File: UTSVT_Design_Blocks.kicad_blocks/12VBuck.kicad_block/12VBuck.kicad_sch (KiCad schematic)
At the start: 9 parts, among them U3 LMR51635XDDCR

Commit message: buck
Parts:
- C11: LCSC # C1607 -> (none); LCSC P/N (none) -> C1607; P/N (none) -> 581-0603YC225MAT2A
- C12: footprint Capacitor_SMD:C_0603_1608Metric_Pad1.08x0.95mm_HandSolder -> Resistor_SMD:R_0201_0603Metric_Pad0.64x0.40mm_HandSolder; LCSC # C440198 -> (none); LCSC P/N (none) -> C14663
- C13: footprint (none) -> Capacitor_SMD:C_0603_1608Metric_Pad1.08x0.95mm_HandSolder
- C14: footprint Capacitor_SMD:C_1210_3225Metric_Pad1.33x2.70mm_HandSolder -> Capacitor_SMD:C_0805_2012Metric_Pad1.18x1.45mm_HandSolder; LCSC P/N (none) -> C440198; P/N 81-GGM32ED70J476KE2L -> GRM21BR61H106KE43K
- C15: footprint Capacitor_SMD:C_1210_3225Metric_Pad1.33x2.70mm_HandSolder -> Capacitor_SMD:C_0805_2012Metric_Pad1.18x1.45mm_HandSolder; LCSC P/N (none) -> C5674; P/N 81-GGM32ED70J476KE2L -> 603-CC805MFX5R5BB226
- L3: footprint Inductor_SMD:L_Sunlord_SWPA4020S -> Inductor_SMD:L_Cenker_CKCS4030; LCSC # C88247 -> (none); LCSC P/N (none) -> C354591; P/N (none) -> 504-HPAL1V1265-150-R
- R1: value 143 -> 143k; footprint Resistor_SMD:R_0805_2012Metric_Pad1.20x1.40mm_HandSolder -> Resistor_SMD:R_0201_0603Metric_Pad0.64x0.40mm_HandSolder; LCSC P/N (none) -> C22877; P/N 667-ERJ-UP6F1430V -> 603-RT0603DRE07143KL; now fitted
- R4: footprint Capacitor_SMD:C_0402_1005Metric_Pad0.74x0.62mm_HandSolder -> Resistor_SMD:R_0201_0603Metric_Pad0.64x0.40mm_HandSolder; LCSC # C11660 -> (none); LCSC P/N (none) -> C22772; P/N (none) -> 603-RT0603DRE0710K2L; now fitted
- U3: LCSC P/N (none) -> C42432812; P/N (none) -> 595-LMR51635XDDCR
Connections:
- net V_in renamed V_in_24V
- net V_out renamed V_out_12V

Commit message: made changes
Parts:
- removed C13: C_Small, Capacitor_SMD:C_0603_1608Metric_Pad1.08x0.95mm_HandSolder, symbol Device:C_Small
- removed C14: 10u, Capacitor_SMD:C_0805_2012Metric_Pad1.18x1.45mm_HandSolder, symbol Device:C_Small
- removed C15: 22u, Capacitor_SMD:C_0805_2012Metric_Pad1.18x1.45mm_HandSolder, symbol Device:C_Small
- added C10, C9: 47u, Capacitor_SMD:C_1210_3225Metric_Pad1.33x2.70mm_HandSolder, symbol Device:C_Small
- C11: footprint Capacitor_SMD:C_0603_1608Metric_Pad1.08x0.95mm_HandSolder -> Capacitor_SMD:C_0805_2012Metric_Pad1.18x1.45mm_HandSolder; LCSC P/N C1607 -> C1771; P/N 581-0603YC225MAT2A -> 963-T21GCB7225MTPA1J
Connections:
- net GND: now also C10.2, C9.2
- net V_out_12V: now also C10.1, C9.1
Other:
- moved on the sheet: R1, R4

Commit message: review addressed
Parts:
- C10, C9: P/N 963-MLAST32MAB5476MP -> GRM32ER61C476KE15L
- C11: P/N 963-T21GCB7225MTPA1J -> CL21F225ZAFNNNE
- L3: footprint Inductor_SMD:L_Cenker_CKCS4030 -> Inductor_SMD:L_TDK_VLP8040; LCSC P/N C354591 -> C2849555; P/N 504-HPAL1V1265-150-R -> PNLS8040-150M 15UH
- R1: P/N 603-RT0603DRE07143KL -> 0603WAF1433T5E
- R4: P/N 603-RT0603DRE0710K2L -> 0603WAF1022T5E
- U3: footprint breh:DDC0006A-MFG -> utsvt_ics:DDC0006A-MFG; P/N 595-LMR51635XDDCR -> LMR51635XDDCR
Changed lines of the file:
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@@
 			)
 		)
-		(property "P/N" "963-MLAST32MAB5476MP"
+		(property "P/N" "GRM32ER61C476KE15L"
 			(at 170.18 90.17 0)
 			(effects
@@
 			)
 		)
-		(property "P/N" "963-T21GCB7225MTPA1J"
+		(property "P/N" "CL21F225ZAFNNNE"
 			(at 93.98 86.36 0)
 			(effects
@@
 			)
 		)
-		(property "Footprint" "Inductor_SMD:L_Cenker_CKCS4030"
+		(property "Footprint" "Inductor_SMD:L_TDK_VLP8040"
 			(at 161.29 86.36 0)
 			(effects
@@
 			)
 		)
-		(property "LCSC P/N" "C354591"
+		(property "LCSC P/N" "C2849555"
 			(at 161.29 86.36 90)
 			(effects
@@
 			)
 		)
-		(property "P/N" "504-HPAL1V1265-150-R"
+		(property "P/N" "PNLS8040-150M 15UH"
 			(at 161.29 86.36 90)
 			(effects
@@
 			)
 		)
-		(property "Footprint" "breh:DDC0006A-MFG"
+		(property "Footprint" "utsvt_ics:DDC0006A-MFG"
 			(at 114.3 81.28 0)
 			(effects
@@
 			)
 		)
-		(property "P/N" "595-LMR51635XDDCR"
+		(property "P/N" "LMR51635XDDCR"
 			(at 114.3 81.28 0)
 			(effects
@@
 			)
 		)
-		(property "P/N" "963-MLAST32MAB5476MP"
+		(property "P/N" "GRM32ER61C476KE15L"
 			(at 181.61 90.17 0)
 			(effects
@@
 			)
 		)
-		(property "P/N" "603-RT0603DRE07143KL"
+		(property "P/N" "0603WAF1433T5E"
 			(at 224.79 86.36 0)
 			(effects
@@
 			)
 		)
-		(property "P/N" "603-RT0603DRE0710K2L"
+		(property "P/N" "0603WAF1022T5E"
 			(at 224.79 93.98 0)
 			(effects

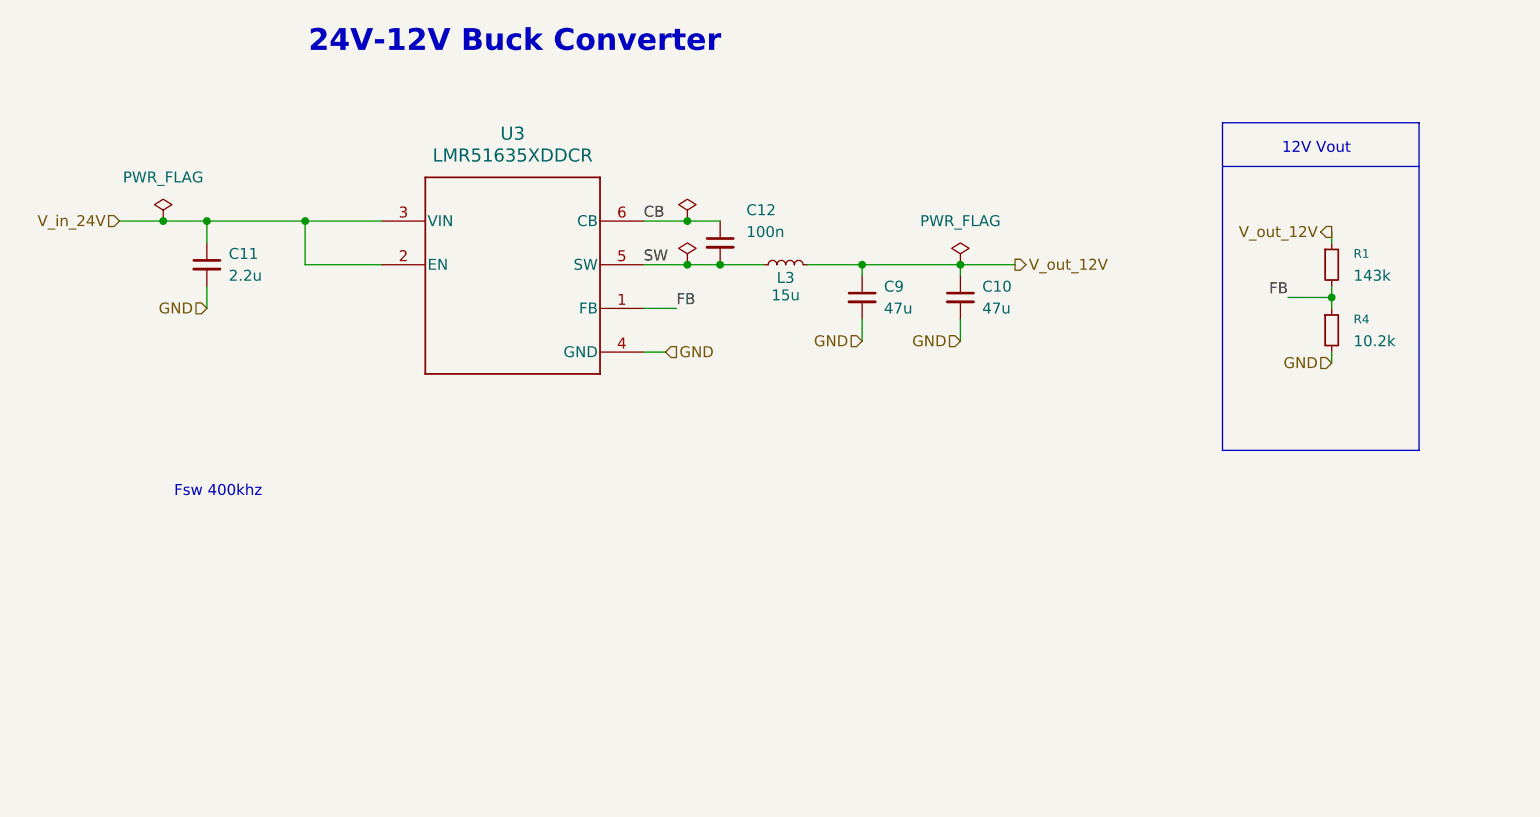
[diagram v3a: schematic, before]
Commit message: fixed designators
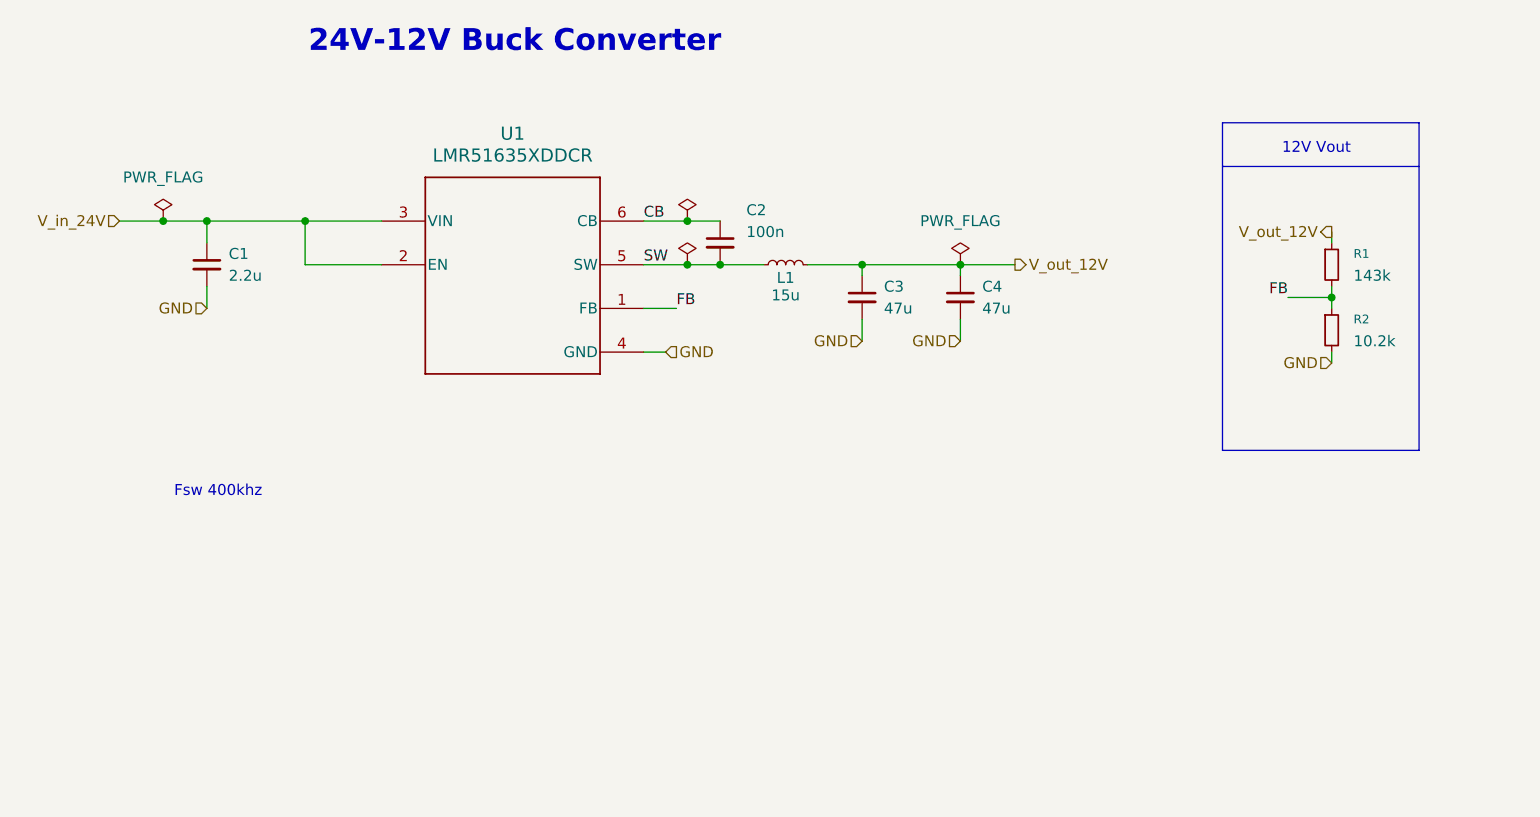
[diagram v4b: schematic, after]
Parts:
- renumbered C11 to C1, C12 to C2, C9 to C3, C10 to C4, L3 to L1, R4 to R2, U3 to U1
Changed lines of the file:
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@@
 		(dnp no)
 		(fields_autoplaced yes)
-		(property "Reference" "C9"
+		(property "Reference" "C3"
 			(at 172.72 88.9062 0)
 			(effects
@@
 				(path "/331f457b-ed4e-4d4a-ad6d-c8acb2febfed/9243f342-8d42-4433-b049-031be1288812"
 					(reference "C9")
+					(unit 1)
+				)
+			)
+			(project "12VBuck"
+				(path "/f2a6729b-b8d5-4133-ae64-a5e680928255"
+					(reference "C3")
 					(unit 1)
 				)
@@
 		(dnp no)
 		(fields_autoplaced yes)
-		(property "Reference" "#FLG013"
+		(property "Reference" "#FLG02"
 			(at 149.86 79.375 0)
 			(effects
@@
 				(path "/331f457b-ed4e-4d4a-ad6d-c8acb2febfed/9243f342-8d42-4433-b049-031be1288812"
 					(reference "#FLG013")
+					(unit 1)
+				)
+			)
+			(project "12VBuck"
+				(path "/f2a6729b-b8d5-4133-ae64-a5e680928255"
+					(reference "#FLG02")
 					(unit 1)
 				)
@@
 		(dnp no)
 		(fields_autoplaced yes)
-		(property "Reference" "C11"
+		(property "Reference" "C1"
 			(at 96.52 85.0962 0)
 			(effects
@@
 				(path "/331f457b-ed4e-4d4a-ad6d-c8acb2febfed/9243f342-8d42-4433-b049-031be1288812"
 					(reference "C11")
+					(unit 1)
+				)
+			)
+			(project "12VBuck"
+				(path "/f2a6729b-b8d5-4133-ae64-a5e680928255"
+					(reference "C1")
 					(unit 1)
 				)
@@
 		(on_board yes)
 		(dnp no)
-		(property "Reference" "L3"
+		(property "Reference" "L1"
 			(at 161.29 87.884 90)
 			(effects
@@
 				(path "/331f457b-ed4e-4d4a-ad6d-c8acb2febfed/9243f342-8d42-4433-b049-031be1288812"
 					(reference "L3")
+					(unit 1)
+				)
+			)
+			(project "12VBuck"
+				(path "/f2a6729b-b8d5-4133-ae64-a5e680928255"
+					(reference "L1")
 					(unit 1)
 				)
@@
 		(dnp no)
 		(fields_autoplaced yes)
-		(property "Reference" "U3"
+		(property "Reference" "U1"
 			(at 129.54 71.12 0)
 			(effects
@@
 				(path "/331f457b-ed4e-4d4a-ad6d-c8acb2febfed/9243f342-8d42-4433-b049-031be1288812"
 					(reference "U3")
+					(unit 1)
+				)
+			)
+			(project "12VBuck"
+				(path "/f2a6729b-b8d5-4133-ae64-a5e680928255"
+					(reference "U1")
 					(unit 1)
 				)
@@
 		(dnp no)
 		(fields_autoplaced yes)
-		(property "Reference" "C10"
+		(property "Reference" "C4"
 			(at 184.15 88.9062 0)
 			(effects
@@
 				(path "/331f457b-ed4e-4d4a-ad6d-c8acb2febfed/9243f342-8d42-4433-b049-031be1288812"
 					(reference "C10")
+					(unit 1)
+				)
+			)
+			(project "12VBuck"
+				(path "/f2a6729b-b8d5-4133-ae64-a5e680928255"
+					(reference "C4")
 					(unit 1)
 				)
@@
 		(dnp no)
 		(fields_autoplaced yes)
-		(property "Reference" "#FLG015"
+		(property "Reference" "#FLG04"
 			(at 181.61 84.455 0)
 			(effects
@@
 				(path "/331f457b-ed4e-4d4a-ad6d-c8acb2febfed/9243f342-8d42-4433-b049-031be1288812"
 					(reference "#FLG015")
+					(unit 1)
+				)
+			)
+			(project "12VBuck"
+				(path "/f2a6729b-b8d5-4133-ae64-a5e680928255"
+					(reference "#FLG04")
 					(unit 1)
 				)
@@
 		(dnp no)
 		(fields_autoplaced yes)
-		(property "Reference" "#FLG011"
+		(property "Reference" "#FLG01"
 			(at 88.9 79.375 0)
 			(effects
@@
 				(path "/331f457b-ed4e-4d4a-ad6d-c8acb2febfed/9243f342-8d42-4433-b049-031be1288812"
 					(reference "#FLG011")
+					(unit 1)
+				)
+			)
+			(project "12VBuck"
+				(path "/f2a6729b-b8d5-4133-ae64-a5e680928255"
+					(reference "#FLG01")
 					(unit 1)
 				)
@@
 		(on_board yes)
 		(dnp no)
-		(property "Reference" "C12"
+		(property "Reference" "C2"
 			(at 156.718 80.01 0)
 			(effects
@@
 				(path "/331f457b-ed4e-4d4a-ad6d-c8acb2febfed/9243f342-8d42-4433-b049-031be1288812"
 					(reference "C12")
+					(unit 1)
+				)
+			)
+			(project "12VBuck"
+				(path "/f2a6729b-b8d5-4133-ae64-a5e680928255"
+					(reference "C2")
 					(unit 1)
 				)
@@
 		(on_board yes)
 		(dnp no)
-		(property "Reference" "#FLG014"
+		(property "Reference" "#FLG03"
 			(at 149.86 84.455 0)
 			(effects
@@
 				(path "/331f457b-ed4e-4d4a-ad6d-c8acb2febfed/9243f342-8d42-4433-b049-031be1288812"
 					(reference "#FLG014")
+					(unit 1)
+				)
+			)
+			(project "12VBuck"
+				(path "/f2a6729b-b8d5-4133-ae64-a5e680928255"
+					(reference "#FLG03")
 					(unit 1)
 				)
@@
 				)
 			)
+			(project "12VBuck"
+				(path "/f2a6729b-b8d5-4133-ae64-a5e680928255"
+					(reference "R1")
+					(unit 1)
+				)
+			)
 		)
 	)
@@
 		(dnp no)
 		(fields_autoplaced yes)
-		(property "Reference" "R4"
+		(property "Reference" "R2"
 			(at 227.33 92.7099 0)
 			(effects
@@
 				)
 			)
-		)
-	)
+			(project "12VBuck"
+				(path "/f2a6729b-b8d5-4133-ae64-a5e680928255"
+					(reference "R2")
+					(unit 1)
+				)
+			)
+		)
+	)
+	(sheet_instances
+		(path "/"
+			(page "1")
+		)
+	)
+	(embedded_fonts no)
 )

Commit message: updated 12V/3V buck resistor footprint + added test points (#57)
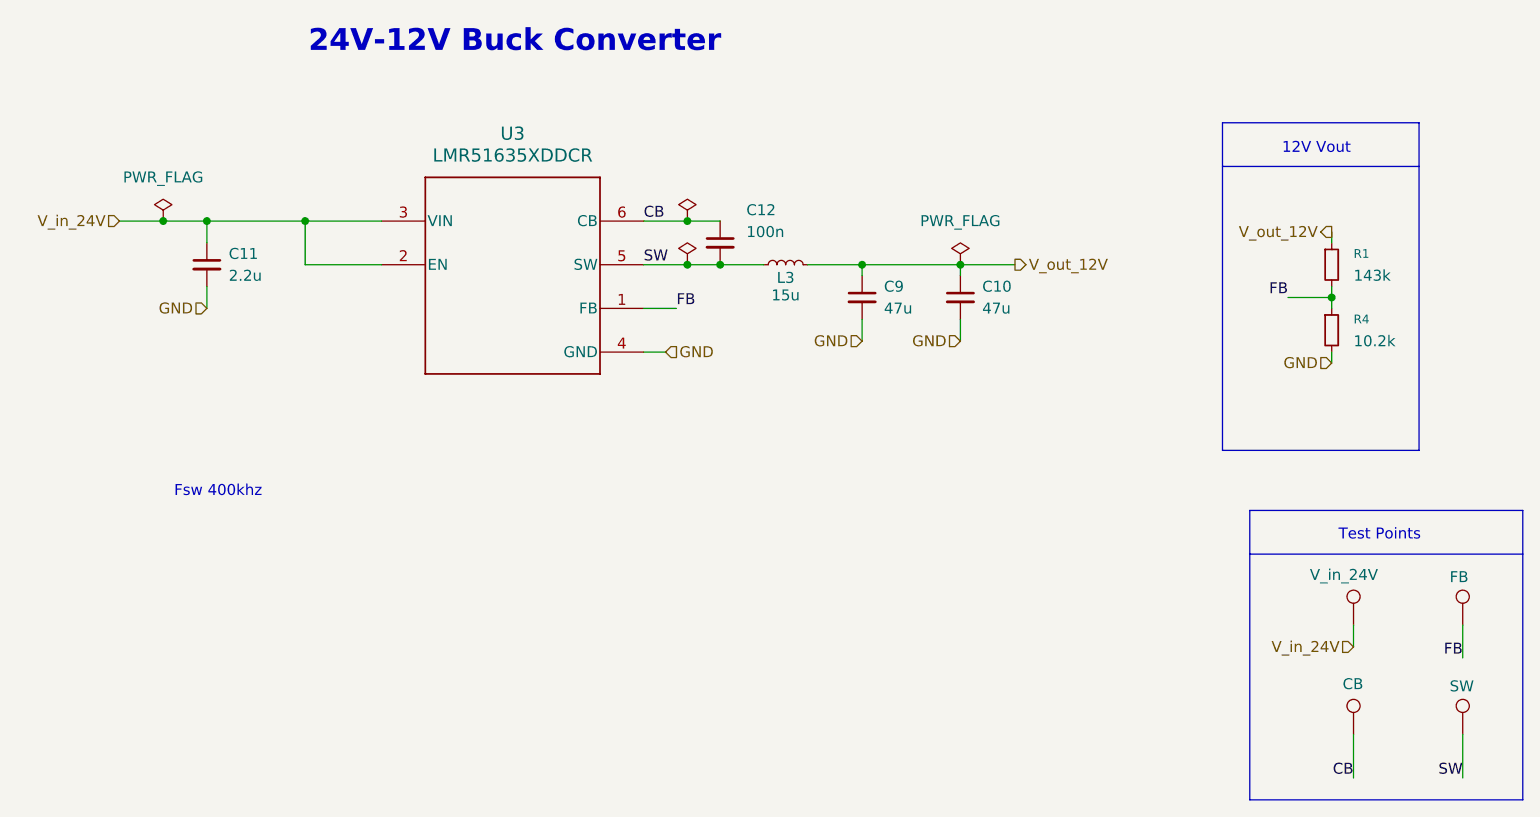
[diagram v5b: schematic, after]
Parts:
- added TP11: CB, TestPoint:TestPoint_THTPad_D3.0mm_Drill1.5mm, symbol Connector:TestPoint
- added TP14: FB, TestPoint:TestPoint_THTPad_D3.0mm_Drill1.5mm, symbol Connector:TestPoint
- added TP15: SW, TestPoint:TestPoint_THTPad_D3.0mm_Drill1.5mm, symbol Connector:TestPoint
- added TP9: V_in_24V, TestPoint:TestPoint_THTPad_D3.0mm_Drill1.5mm, symbol Connector:TestPoint
- R1: footprint Resistor_SMD:R_0201_0603Metric_Pad0.64x0.40mm_HandSolder -> Resistor_SMD:R_0603_1608Metric
- R4: renamed from R2; footprint Resistor_SMD:R_0201_0603Metric_Pad0.64x0.40mm_HandSolder -> Resistor_SMD:R_0603_1608Metric
- renumbered C4 to C10, C1 to C11, C2 to C12, C3 to C9, L1 to L3, U1 to U3
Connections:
- net CB: now also TP11.1
- net FB: now also TP14.1
- net SW: now also TP15.1
- net V_in_24V: now also TP9.1
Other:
- note added: "Test Points"
